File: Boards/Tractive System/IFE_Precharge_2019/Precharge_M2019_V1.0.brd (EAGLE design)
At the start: 39.4 x 45.7 mm, 21 parts

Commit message: More precharge organization
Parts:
- RSET: value 350k -> 220k; device SparkFun-Resistors:AXIAL-0.5 -> rcl:0207/10
- moved RSET 6.74 mm to (12.1, 2.16), turned to 0 degrees
- moved C1 2.54 mm to (32.5, 10.0)
- moved U$1 2.54 mm to (20.8, 15.2)
- moved RDIST 2.05 mm to (32.8, 21.3)
- moved R6 1.45 mm to (33.0, 31.4)
- moved R5 1.40 mm to (33.0, 35.4)
- moved D1 1.40 mm to (24.3, 2.16)
- moved AIR_ON 1.27 mm to (30.0, 41.9)
- moved PRECHARGE 1.27 mm to (26.4, 41.9)
- moved U$3 1.27 mm to (8.38, 24.9)
- moved U$5 1.05 mm to (28.2, 34.5)
- moved U$6 1.02 mm to (28.2, 30.5)
- moved R2 0.77 mm to (24.6, 35.7)
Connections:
- net N$1: now also RSET.1; no longer RSET.P$1
- net V+: now also RSET.2; no longer RSET.P$2
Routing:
- net N$1: track 7.54 -> 21.8 mm
- net V+: track 100.2 -> 92.6 mm
- net N$2: track 38.9 -> 37.1 mm
- net PRECHARGE_COMPLETE: track 42.8 -> 41.7 mm
- net N$4: track 22.1 -> 21.4 mm
- net PRECHARGE: track 22.5 -> 22.0 mm, vias 3 -> 4
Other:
- board size 39.4 x 45.7 mm -> 36.8 x 45.7 mm

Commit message: More precharge organization
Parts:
- moved AIR_ON 1.27 mm to (28.7, 41.9)
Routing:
- net N$5: track 8.22 -> 8.75 mm
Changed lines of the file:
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@@
 <hole x="33.02" y="3.81" drill="2.8956"/>
 <hole x="33.02" y="41.91" drill="2.8956"/>
-<text x="29.972" y="38.989" size="0.8128" layer="25" align="center">AIR
+<text x="28.702" y="38.989" size="0.8128" layer="25" align="center">AIR
 ON</text>
-<text x="24.384" y="39.116" size="0.8128" layer="25" align="center">PRECHARGE
+<text x="23.622" y="39.116" size="0.8128" layer="25" align="center">PRECHARGE
 COMPLETE</text>
-<text x="16.51" y="43.18" size="1.778" layer="25" align="center">IFE PRECHARGE</text>
-<text x="12.319" y="41.021" size="1.27" layer="25" align="center">M2019 v1.0</text>
+<text x="15.24" y="43.18" size="1.778" layer="25" align="center">IFE PRECHARGE</text>
+<text x="11.43" y="41.021" size="1.27" layer="25" align="center">M2019 v1.0</text>
 </plain>
 <attributes>
@@
 <attribute name="SPICEPREFIX" value="R" x="33.02" y="31.369" size="1.778" layer="27" display="off"/>
 </element>
-<element name="AIR_ON" library="SparkFun-LED" package="LED-0603" value="" x="29.972" y="41.91" smashed="yes" rot="R180">
-<attribute name="VALUE" x="28.8925" y="42.926" size="0.4064" layer="27" rot="R270"/>
+<element name="AIR_ON" library="SparkFun-LED" package="LED-0603" value="" x="28.702" y="41.91" smashed="yes" rot="R180">
+<attribute name="VALUE" x="27.6225" y="42.926" size="0.4064" layer="27" rot="R270"/>
 </element>
 <element name="PRECHARGE" library="SparkFun-LED" package="LED-0603" value="" x="26.416" y="41.91" smashed="yes" rot="R180">
@@
 <contactref element="AIR_ON" pad="A"/>
 <via x="32.07" y="35.433" extent="1-16" drill="0.35"/>
-<via x="29.972" y="42.787" extent="1-16" drill="0.35"/>
-<wire x1="32.07" y1="35.433" x2="30.734" y2="36.769" width="0.4064" layer="16"/>
-<wire x1="30.734" y1="42.025" x2="29.972" y2="42.787" width="0.4064" layer="16"/>
-<wire x1="30.734" y1="36.769" x2="30.734" y2="42.025" width="0.4064" layer="16"/>
+<via x="28.702" y="42.787" extent="1-16" drill="0.35"/>
+<wire x1="32.07" y1="35.433" x2="29.8528" y2="37.6502" width="0.4064" layer="16"/>
+<wire x1="28.702" y1="41.9989125" x2="28.702" y2="42.787" width="0.4064" layer="16"/>
+<wire x1="29.8528" y1="40.8481125" x2="28.702" y2="41.9989125" width="0.4064" layer="16"/>
+<wire x1="29.8528" y1="37.6502" x2="29.8528" y2="40.8481125" width="0.4064" layer="16"/>
 </signal>
 <signal name="N$6">
@@
 <contactref element="AIR_ON" pad="C"/>
 <contactref element="U$5" pad="3"/>
-<via x="29.972" y="41.033" extent="1-16" drill="0.35"/>
+<via x="28.702" y="41.033" extent="1-16" drill="0.35"/>
 <via x="29.294" y="34.544" extent="1-16" drill="0.35"/>
-<wire x1="29.972" y1="41.033" x2="29.294" y2="40.355" width="0.4064" layer="16"/>
-<wire x1="29.294" y1="40.355" x2="29.294" y2="34.544" width="0.4064" layer="16"/>
+<wire x1="28.702" y1="41.033" x2="29.294" y2="40.441" width="0.4064" layer="16"/>
+<wire x1="29.294" y1="40.441" x2="29.294" y2="34.544" width="0.4064" layer="16"/>
 </signal>
 </signals>

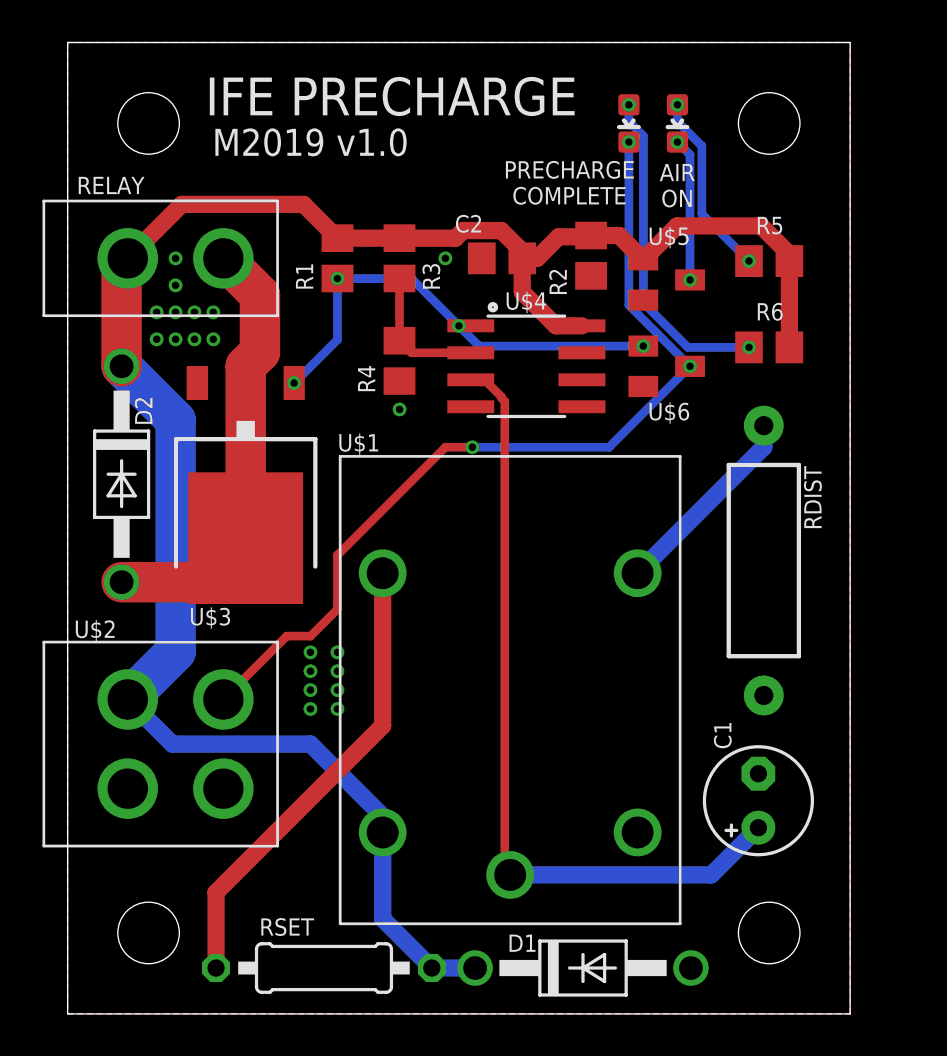
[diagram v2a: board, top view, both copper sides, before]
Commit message: Adjusted precharge relay package, reduced area
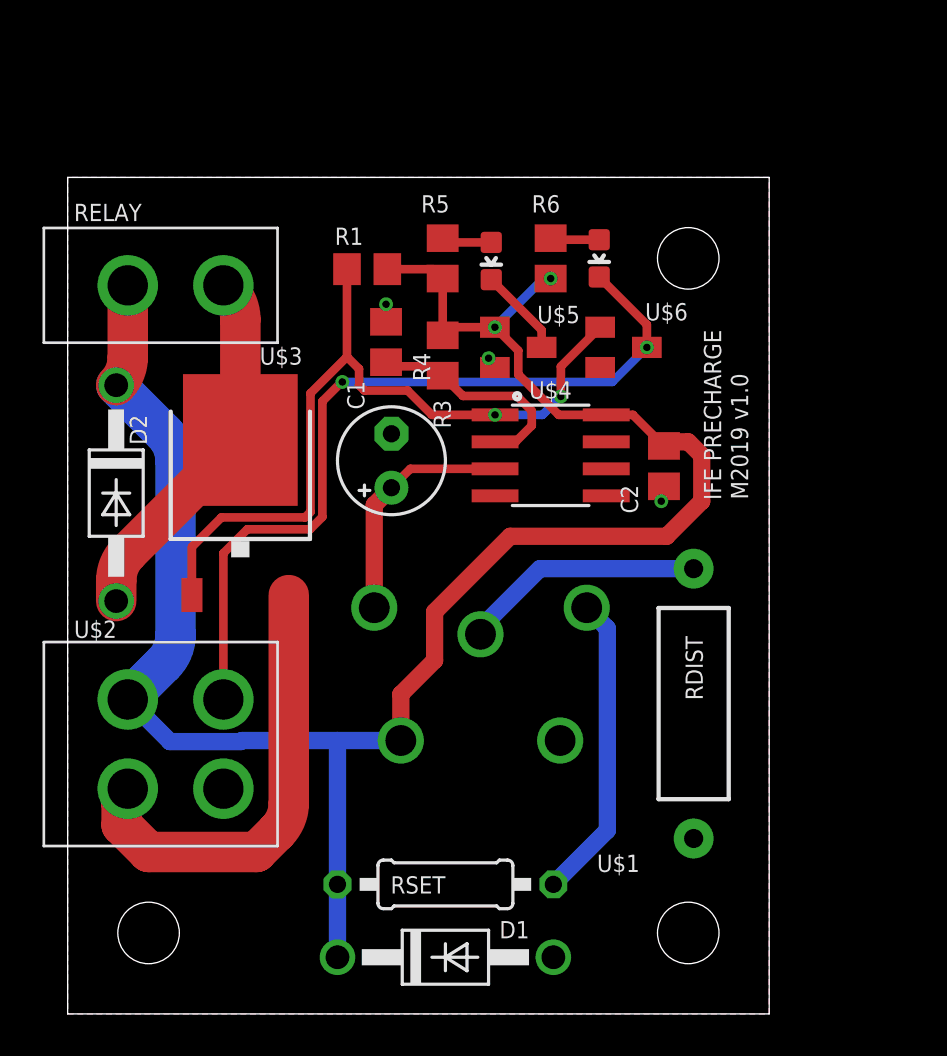
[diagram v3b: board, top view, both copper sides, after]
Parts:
- removed R2: 10k, rcl:R0805
- U$1: value JS-M -> PB114012; device Display_Custom:JS-M.1C -> Display_Custom:TH_SPDT_MINI_POWER_RELAY_PB
- moved C1 23.5 mm to (15.2, 26.0)
- moved R5 15.4 mm to (17.7, 35.6), turned to 270 degrees
- moved C2 12.4 mm to (28.1, 25.8), turned to 270 degrees
- moved R6 11.1 mm to (22.7, 35.6), turned to 270 degrees
- moved AIR_ON 10.9 mm to (19.9, 35.4)
- moved U$5 7.67 mm to (21.2, 31.4)
- moved RDIST 7.50 mm to (29.5, 14.6)
- moved RSET 6.94 mm to (17.8, 6.10), turned to 180 degrees
- moved PRECHARGE 6.50 mm to (25.0, 35.6)
- moved D1 6.50 mm to (17.8, 2.67)
- moved R3 5.00 mm to (17.7, 31.0)
- moved U$4 4.34 mm to (22.7, 26.3)
- moved U$6 2.22 mm to (26.2, 31.4)
- moved R1 1.49 mm to (14.1, 35.1), turned to 0 degrees
- moved U$1 1.40 mm to (19.4, 15.4)
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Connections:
- net GND: now also U$1.A2; no longer R2.1, U$1.P$5
- net N$1: now also U$1.14; no longer U$1.P$3
- net N$2: now also U$1.11; no longer U$1.P$1
- net N$3: now also U$1.12; no longer U$1.P$4
- net V+: now also U$1.A1; no longer R2.2, U$1.P$2
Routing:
- net N$2: track 37.1 -> 11.2 mm
- net GND: track 0.00 -> 22.0 mm, vias 20 -> 3
- net PRECHARGE: track 22.0 -> 36.7 mm, vias 4 -> 2
- net N$6: track 15.4 -> 2.32 mm, vias 2 -> 0
- net N$1: track 21.8 -> 14.5 mm
- net N$5: track 8.75 -> 2.37 mm, vias 2 -> 0
- net N$4: track 21.4 -> 17.4 mm
- net V_TRIG: track 6.51 -> 10.5 mm
- net PRECHARGE_COMPLETE: track 41.7 -> 38.3 mm, vias 3 -> 2
- net N$9: track 6.73 -> 4.17 mm, vias 2 -> 0
- net N$3: track 9.41 -> 11.5 mm
- net V+: track 92.6 -> 93.6 mm, vias 0 -> 2
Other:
- board size 36.8 x 45.7 mm -> 33 x 39.4 mm
- board text removed: "AIR ON"
- board text removed: "PRECHARGE COMPLETE"

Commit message: Adding circuitry to shutdown, relay drivers
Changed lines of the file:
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@@
 <?xml version="1.0" encoding="utf-8"?>
 <!DOCTYPE eagle SYSTEM "eagle.dtd">
-<eagle version="8.7.0">
+<eagle version="9.1.1">
 <drawing>
 <settings>
@@
 <param name="checkStop" value="0"/>
 <param name="checkValues" value="0"/>
+<param name="checkNames" value="1"/>
+<param name="checkWireStubs" value="1"/>
+<param name="checkPolygonWidth" value="0"/>
 <param name="useDiameter" value="13"/>
 <param name="maxErrors" value="50"/>
@@
 </element>
 <element name="U$6" library="Display_Custom" package="SOT23" value="DMN65D8L" x="26.162" y="31.369" smashed="yes" rot="R270">
-<attribute name="NAME" x="27.178" y="32.639" size="0.8128" layer="25"/>
+<attribute name="NAME" x="28.448" y="32.639" size="0.8128" layer="25"/>
 </element>
 <element name="R5" library="rcl" library_urn="urn:adsk.eagle:library:334" package="R0805" package3d_urn="urn:adsk.eagle:package:23553/2" value="1k" x="17.653" y="35.56" smashed="yes" rot="R270">
@@
 </signal>
 </signals>
+<mfgpreviewcolors>
+<mfgpreviewcolor name="soldermaskcolor" color="0xC8008000"/>
+<mfgpreviewcolor name="silkscreencolor" color="0xFFFEFEFE"/>
+<mfgpreviewcolor name="backgroundcolor" color="0xFF282828"/>
+<mfgpreviewcolor name="coppercolor" color="0xFFFFBF00"/>
+<mfgpreviewcolor name="substratecolor" color="0xFF786E46"/>
+</mfgpreviewcolors>
 </board>
 </drawing>
